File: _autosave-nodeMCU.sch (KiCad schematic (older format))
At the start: 38 parts, among them J1 USB_B_Micro, J2 Conn_01x15, J3 Conn_01x15, Q1 S8050, Q2 S8050, SW1 RESET, SW2 FLASH, U1 AP1117-33, U2 CP2102N-A01-GQFN28, U3 ESP-12E

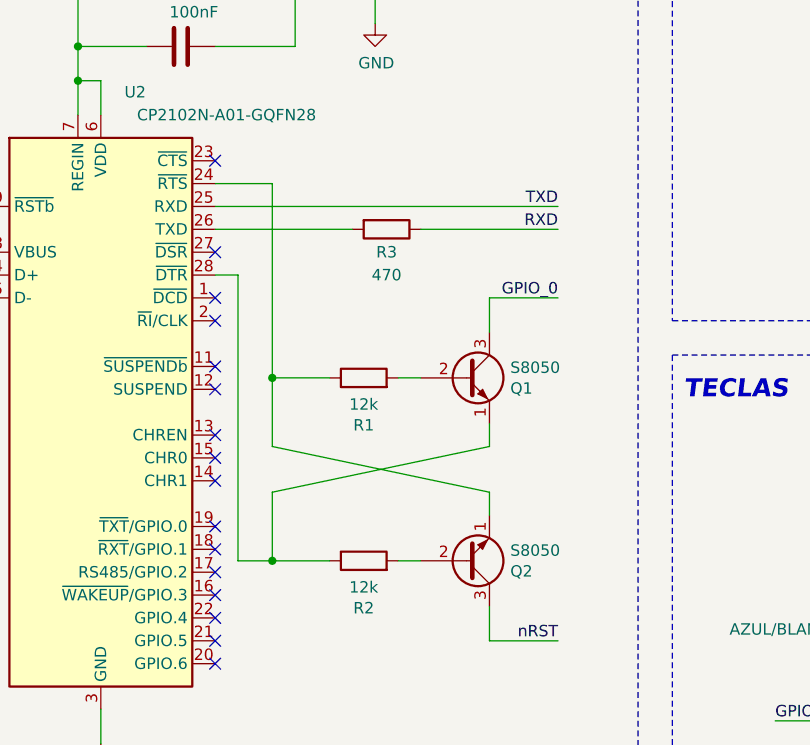
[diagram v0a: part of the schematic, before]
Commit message: Termino el ruteo
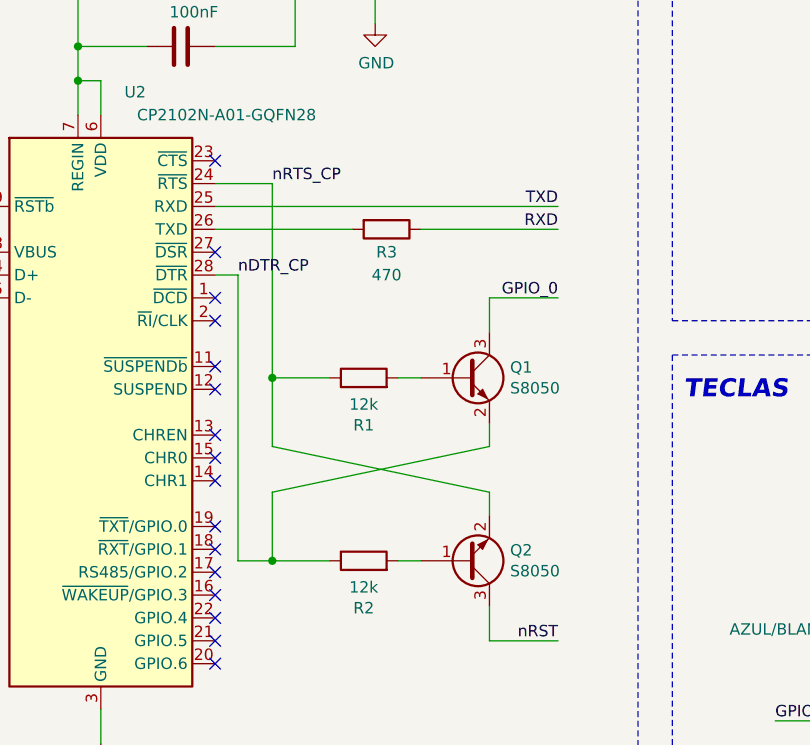
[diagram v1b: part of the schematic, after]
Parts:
- removed Q1, Q2: S8050, Package_TO_SOT_SMD:SOT-23, symbol Transistor_BJT:S8050
- added Q1, Q2: S8050, Package_TO_SOT_SMD:SOT-23, symbol Device:Q_NPN_BEC
- J1: footprint Connector_USB:USB_Micro-B_Amphenol_10103594-0001LF_Horizontal -> Connector_USB:USB_Micro-B_Molex-105017-0001
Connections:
- net GPIO_0: now also Q1.3 (C)
- net nRST: now also Q2.3 (C)
- net nRTS_CP: now reaches R1.1, U2.24 (~RTS)
- net nRTS_CP: now also Q2.2 (E)
- net nDTR_CP: now reaches R2.1, U2.28 (~DTR)
- net nDTR_CP: now also Q1.2 (E)
- net at R2.2: now also Q2.1 (B)
- net at R1.2: now also Q1.1 (B)
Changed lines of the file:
@@
 $EndDescr
-$Comp
-L Transistor_BJT:S8050 Q2
-U 1 1 5D014577
-P 4950 4400
-F 0 "Q2" H 5141 4446 50  0000 L CNN
-F 1 "S8050" H 5141 4355 50  0000 L CNN
-F 2 "Package_TO_SOT_SMD:SOT-23" H 5150 4325 50  0001 L CIN
-F 3 "http://www.unisonic.com.tw/datasheet/S8050.pdf" H 4950 4400 50  0001 L CNN
-	1    4950 4400
-	1    0    0    1
-$EndComp
-$Comp
-L Transistor_BJT:S8050 Q1
-U 1 1 5D0158DF
-P 4950 3600
-F 0 "Q1" H 5141 3554 50  0000 L CNN
-F 1 "S8050" H 5141 3645 50  0000 L CNN
-F 2 "Package_TO_SOT_SMD:SOT-23" H 5150 3525 50  0001 L CIN
-F 3 "http://www.unisonic.com.tw/datasheet/S8050.pdf" H 4950 3600 50  0001 L CNN
-	1    4950 3600
-	1    0    0    -1
-$EndComp
 $Comp
 L Device:R R2
@@
 F 0 "J1" H 1307 4517 50  0000 C CNN
 F 1 "USB_B_Micro" H 1307 4426 50  0000 C CNN
-F 2 "Connector_USB:USB_Micro-B_Amphenol_10103594-0001LF_Horizontal" H 1400 4000 50  0001 C CNN
+F 2 "Connector_USB:USB_Micro-B_Molex-105017-0001" H 1400 4000 50  0001 C CNN
 F 3 "~" H 1400 4000 50  0001 C CNN
 	1    1250 4050
 	1    0    0    -1
 $EndComp
+Text Label 4100 2750 0    50   ~ 0
+nRTS_CP
+Text Label 3950 3150 0    50   ~ 0
+nDTR_CP
+$Comp
+L Device:Q_NPN_BEC Q1
+U 1 1 5D1876D5
+P 4950 3600
+F 0 "Q1" H 5140 3646 50  0000 L CNN
+F 1 "S8050" H 5140 3555 50  0000 L CNN
+F 2 "Package_TO_SOT_SMD:SOT-23" H 5150 3700 50  0001 C CNN
+F 3 "~" H 4950 3600 50  0001 C CNN
+	1    4950 3600
+	1    0    0    -1
+$EndComp
+$Comp
+L Device:Q_NPN_BEC Q2
+U 1 1 5D189887
+P 4950 4400
+F 0 "Q2" H 5140 4354 50  0000 L CNN
+F 1 "S8050" H 5140 4445 50  0000 L CNN
+F 2 "Package_TO_SOT_SMD:SOT-23" H 5150 4500 50  0001 C CNN
+F 3 "~" H 4950 4400 50  0001 C CNN
+	1    4950 4400
+	1    0    0    1
+$EndComp
 $EndSCHEMATC
